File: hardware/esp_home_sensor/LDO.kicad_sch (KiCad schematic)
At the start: 7 parts

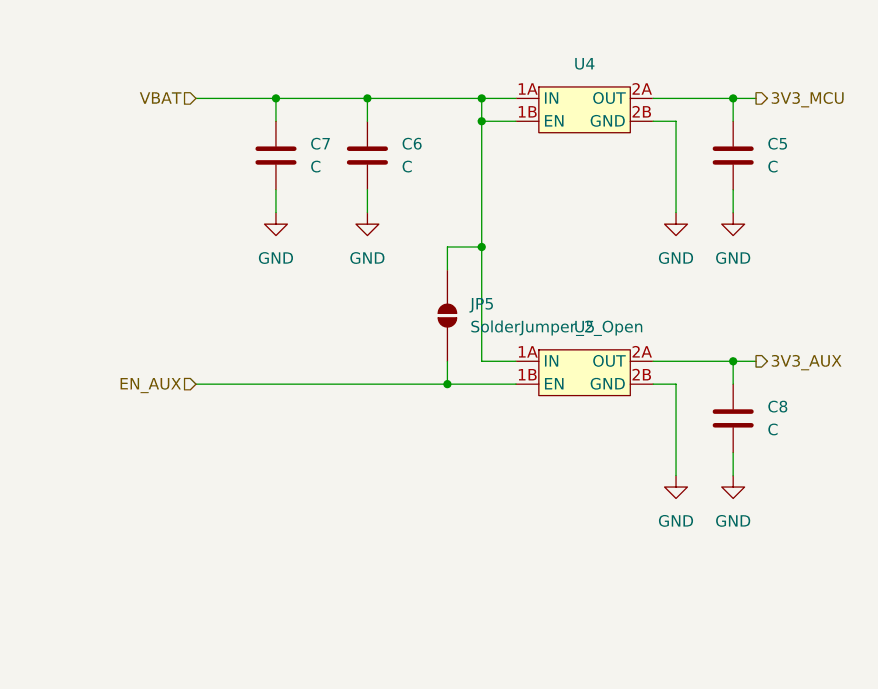
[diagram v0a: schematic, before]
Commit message: footprint assignment, buck
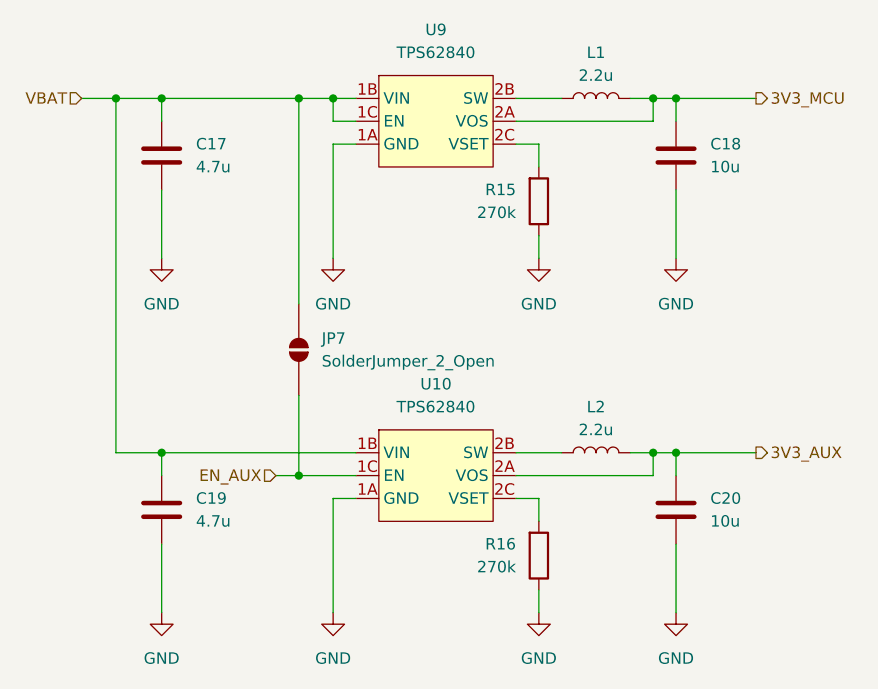
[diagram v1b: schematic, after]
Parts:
- removed C5, C6, C7, C8: C, symbol Device:C
- removed JP5: SolderJumper_2_Open, symbol Jumper:SolderJumper_2_Open
- removed U4, U5: (no value), symbol esp_home_sensor:TPS7A21
- added C17, C19: 4.7u, Capacitor_SMD:C_0402_1005Metric, symbol Device:C
- added C18, C20: 10u, Capacitor_SMD:C_0402_1005Metric, symbol Device:C
- added JP7: SolderJumper_2_Open, symbol Jumper:SolderJumper_2_Open
- added L1, L2: 2.2u, Inductor_SMD:L_0805_2012Metric, symbol Device:L
- added R15, R16: 270k, Resistor_SMD:R_0402_1005Metric, symbol Device:R
- added U10, U9: TPS62840, esp_home_sensor:BGA-6_2x3_1.5x1.2mm, symbol esp_home_sensor:TPS62840
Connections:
- net 3V3_AUX: now also C20.1, L2.2, U10.2A (VOS)
- net 3V3_MCU: now also C18.1, L1.2, U9.2A (VOS)
- net EN_AUX: now also JP7.1 (A), U10.1C (EN)
- net GND: now also C17.2, C18.2, C19.2, C20.2, R15.1, R16.1, U10.1A (GND), U9.1A (GND)
- net VBAT: now also C17.1, C19.1, JP7.2 (B), U10.1B (VIN), U9.1B (VIN), U9.1C (EN)
- new net: R16.2, U10.2C (VSET)
- new net: L2.1, U10.2B (SW)
- new net: L1.1, U9.2B (SW)
- new net: R15.2, U9.2C (VSET)

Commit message: minor update
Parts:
- JP7: footprint (none) -> Jumper:SolderJumper-2_P1.3mm_Open_Pad1.0x1.5mm
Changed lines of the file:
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@@
 			)
 		)
-		(property "Footprint" ""
+		(property "Footprint" "Jumper:SolderJumper-2_P1.3mm_Open_Pad1.0x1.5mm"
 			(at 110.49 132.08 0)
 			(hide yes)
-			(show_name no)
+			(show_name yes)
 			(do_not_autoplace no)
 			(effects

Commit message: initial layout, power routing
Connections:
- net VSET: now reaches R16.2, U10.2C (VSET)
- net VSET: now also R15.2, U9.2C (VSET)
- net SW: now reaches L2.1, U10.2B (SW)
- net SW: now also L1.1, U9.2B (SW)
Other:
- moved on the sheet: R15, R16

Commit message: layout
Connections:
- net SW renamed SW_aux
- net SW_aux: no longer L1.1, U9.2B (SW)
- new net SW_mcu: L1.1, U9.2B (SW)
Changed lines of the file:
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@@
 		)
 	)
-	(label "SW"
+	(label "SW_mcu"
 		(at 139.7 104.14 180)
 		(effects
@@
 		)
 	)
-	(label "SW"
+	(label "SW_aux"
 		(at 139.7 143.51 180)
 		(effects

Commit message: layout
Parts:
- renumbered C17 to C5, C19 to C6, C18 to C7, C20 to C8, JP7 to JP3, R15 to R13, R16 to R14, U9 to U4, U10 to U5
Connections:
- net VSET renamed VSET_aux
- net VSET_aux: no longer R13.2, U4.2C (VSET)
- new net VSET_mcu: R13.2, U4.2C (VSET)
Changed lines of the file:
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@@
 		)
 	)
-	(label "VSET"
+	(label "VSET_aux"
 		(at 139.7 148.59 180)
 		(effects
@@
 		)
 	)
-	(label "VSET"
+	(label "VSET_mcu"
 		(at 139.7 109.22 180)
 		(effects
@@
 		(dnp no)
 		(fields_autoplaced yes)
-		(property "Reference" "C18"
+		(property "Reference" "C7"
 			(at 156.21 109.2199 0)
 			(show_name no)
@@
 			(project "esp_home_sensor"
 				(path "/1b1bee14-8d82-405b-b99d-415549a137e6/e21bf01f-a4a7-4c2d-ae41-3af078114327"
-					(reference "C18")
+					(reference "C7")
 					(unit 1)
 				)
@@
 		(in_pos_files yes)
 		(dnp no)
-		(property "Reference" "#PWR057"
+		(property "Reference" "#PWR032"
 			(at 152.4 167.64 0)
 			(hide yes)
@@
 			(project "esp_home_sensor"
 				(path "/1b1bee14-8d82-405b-b99d-415549a137e6/e21bf01f-a4a7-4c2d-ae41-3af078114327"
-					(reference "#PWR057")
+					(reference "#PWR032")
 					(unit 1)
 				)
@@
 		(dnp no)
 		(fields_autoplaced yes)
-		(property "Reference" "R16"
+		(property "Reference" "R14"
 			(at 137.16 153.6699 0)
 			(show_name no)
@@
 			(project "esp_home_sensor"
 				(path "/1b1bee14-8d82-405b-b99d-415549a137e6/e21bf01f-a4a7-4c2d-ae41-3af078114327"
-					(reference "R16")
+					(reference "R14")
 					(unit 1)
 				)
@@
 		(in_pos_files yes)
 		(dnp no)
-		(property "Reference" "JP7"
+		(property "Reference" "JP3"
 			(at 113.03 130.8099 90)
 			(show_name no)
@@
 			(project "esp_home_sensor"
 				(path "/1b1bee14-8d82-405b-b99d-415549a137e6/e21bf01f-a4a7-4c2d-ae41-3af078114327"
-					(reference "JP7")
+					(reference "JP3")
 					(unit 1)
 				)
@@
 		(dnp no)
 		(fields_autoplaced yes)
-		(property "Reference" "C19"
+		(property "Reference" "C6"
 			(at 99.06 148.5899 0)
 			(show_name no)
@@
 			(project "esp_home_sensor"
 				(path "/1b1bee14-8d82-405b-b99d-415549a137e6/e21bf01f-a4a7-4c2d-ae41-3af078114327"
-					(reference "C19")
+					(reference "C6")
 					(unit 1)
 				)
@@
 		(in_pos_files yes)
 		(dnp no)
-		(property "Reference" "#PWR055"
+		(property "Reference" "#PWR028"
 			(at 114.3 167.64 0)
 			(hide yes)
@@
 			(project "esp_home_sensor"
 				(path "/1b1bee14-8d82-405b-b99d-415549a137e6/e21bf01f-a4a7-4c2d-ae41-3af078114327"
-					(reference "#PWR055")
+					(reference "#PWR028")
 					(unit 1)
 				)
@@
 		(in_pos_files yes)
 		(dnp no)
-		(property "Reference" "#PWR052"
+		(property "Reference" "#PWR027"
 			(at 114.3 128.27 0)
 			(hide yes)
@@
 			(project "esp_home_sensor"
 				(path "/1b1bee14-8d82-405b-b99d-415549a137e6/e21bf01f-a4a7-4c2d-ae41-3af078114327"
-					(reference "#PWR052")
+					(reference "#PWR027")
 					(unit 1)
 				)
@@
 		(in_pos_files yes)
 		(dnp no)
-		(property "Reference" "#PWR054"
+		(property "Reference" "#PWR026"
 			(at 95.25 167.64 0)
 			(hide yes)
@@
 			(project "esp_home_sensor"
 				(path "/1b1bee14-8d82-405b-b99d-415549a137e6/e21bf01f-a4a7-4c2d-ae41-3af078114327"
-					(reference "#PWR054")
+					(reference "#PWR026")
 					(unit 1)
 				)
@@
 		(in_pos_files yes)
 		(dnp no)
-		(property "Reference" "#PWR051"
+		(property "Reference" "#PWR031"
 			(at 152.4 128.27 0)
 			(hide yes)
@@
 			(project "esp_home_sensor"
 				(path "/1b1bee14-8d82-405b-b99d-415549a137e6/e21bf01f-a4a7-4c2d-ae41-3af078114327"
-					(reference "#PWR051")
+					(reference "#PWR031")
 					(unit 1)
 				)
@@
 		(in_pos_files yes)
 		(dnp no)
-		(property "Reference" "#PWR056"
+		(property "Reference" "#PWR030"
 			(at 139.7 167.64 0)
 			(hide yes)
@@
 			(project "esp_home_sensor"
 				(path "/1b1bee14-8d82-405b-b99d-415549a137e6/e21bf01f-a4a7-4c2d-ae41-3af078114327"
-					(reference "#PWR056")
+					(reference "#PWR030")
 					(unit 1)
 				)
@@
 		(dnp no)
 		(fields_autoplaced yes)
-		(property "Reference" "C17"
+		(property "Reference" "C5"
 			(at 99.06 109.2199 0)
 			(show_name no)
@@
 			(project "esp_home_sensor"
 				(path "/1b1bee14-8d82-405b-b99d-415549a137e6/e21bf01f-a4a7-4c2d-ae41-3af078114327"
-					(reference "C17")
+					(reference "C5")
 					(unit 1)
 				)
@@
 		(in_pos_files yes)
 		(dnp no)
-		(property "Reference" "#PWR050"
+		(property "Reference" "#PWR025"
 			(at 95.25 128.27 0)
 			(hide yes)
@@
 			(project "esp_home_sensor"
 				(path "/1b1bee14-8d82-405b-b99d-415549a137e6/e21bf01f-a4a7-4c2d-ae41-3af078114327"
-					(reference "#PWR050")
+					(reference "#PWR025")
 					(unit 1)
 				)
@@
 		(dnp no)
 		(fields_autoplaced yes)
-		(property "Reference" "C20"
+		(property "Reference" "C8"
 			(at 156.21 148.5899 0)
 			(show_name no)
@@
 			(project "esp_home_sensor"
 				(path "/1b1bee14-8d82-405b-b99d-415549a137e6/e21bf01f-a4a7-4c2d-ae41-3af078114327"
-					(reference "C20")
+					(reference "C8")
 					(unit 1)
 				)
@@
 		(in_pos_files yes)
 		(dnp no)
-		(property "Reference" "#PWR053"
+		(property "Reference" "#PWR029"
 			(at 139.7 128.27 0)
 			(hide yes)
@@
 			(project "esp_home_sensor"
 				(path "/1b1bee14-8d82-405b-b99d-415549a137e6/e21bf01f-a4a7-4c2d-ae41-3af078114327"
-					(reference "#PWR053")
+					(reference "#PWR029")
 					(unit 1)
 				)
@@
 		(dnp no)
 		(fields_autoplaced yes)
-		(property "Reference" "U10"
+		(property "Reference" "U5"
 			(at 125.73 135.89 0)
 			(show_name no)
@@
 			(project "esp_home_sensor"
 				(path "/1b1bee14-8d82-405b-b99d-415549a137e6/e21bf01f-a4a7-4c2d-ae41-3af078114327"
-					(reference "U10")
+					(reference "U5")
 					(unit 1)
 				)
@@
 		(dnp no)
 		(fields_autoplaced yes)
-		(property "Reference" "U9"
+		(property "Reference" "U4"
 			(at 125.73 96.52 0)
 			(show_name no)
@@
 			(project "esp_home_sensor"
 				(path "/1b1bee14-8d82-405b-b99d-415549a137e6/e21bf01f-a4a7-4c2d-ae41-3af078114327"
-					(reference "U9")
+					(reference "U4")
 					(unit 1)
 				)
@@
 		(dnp no)
 		(fields_autoplaced yes)
-		(property "Reference" "R15"
+		(property "Reference" "R13"
 			(at 137.16 114.2999 0)
 			(show_name no)
@@
 			(project "esp_home_sensor"
 				(path "/1b1bee14-8d82-405b-b99d-415549a137e6/e21bf01f-a4a7-4c2d-ae41-3af078114327"
-					(reference "R15")
+					(reference "R13")
 					(unit 1)
 				)

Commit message: in production
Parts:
- C5, C6: Mfr. No. (none) -> GRM155C61E475ME15D
- C7, C8: Mfr. No. (none) -> GRM155R61A106ME11D
- R13, R14: Mfr. No. (none) -> RC0402JR-07270KL
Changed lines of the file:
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@@
 			)
 		)
-		(property "Mfr. No." ""
+		(property "Mfr. No." "GRM155R61A106ME11D"
 			(at 152.4 110.49 0)
 			(hide yes)
@@
 			)
 		)
-		(property "Mfr. No." ""
+		(property "Mfr. No." "RC0402JR-07270KL"
 			(at 139.7 154.94 90)
 			(hide yes)
@@
 			)
 		)
-		(property "Mfr. No." ""
+		(property "Mfr. No." "GRM155C61E475ME15D"
 			(at 95.25 149.86 0)
 			(hide yes)
@@
 			)
 		)
-		(property "Mfr. No." ""
+		(property "Mfr. No." "GRM155C61E475ME15D"
 			(at 95.25 110.49 0)
 			(hide yes)
@@
 			)
 		)
-		(property "Mfr. No." ""
+		(property "Mfr. No." "GRM155R61A106ME11D"
 			(at 152.4 149.86 0)
 			(hide yes)
@@
 			)
 		)
-		(property "Mfr. No." ""
+		(property "Mfr. No." "RC0402JR-07270KL"
 			(at 139.7 115.57 90)
 			(hide yes)

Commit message: az
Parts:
- U4, U5: Down_current (none) -> 120n; Supply_current (none) -> 120n
